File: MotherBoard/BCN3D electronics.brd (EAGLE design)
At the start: 70.5 x 95.8 mm, 87 parts, among them IC2 FT232RL, Q2 IRLS3034

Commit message: New File Tree and Updates
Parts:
- added DRILEGEND: (no value), drilegend:DRILEGEND
- U$5: device MarcEagleParts:SIGMA_LOGO -> MarcEagleParts:BCN3D_LOGO
- moved FID3 47.9 mm to (23.6, 9.93)
- moved LOGO1 21.3 mm to (16.1, 33.2)
- moved FID2 9.09 mm to (46.6, 79.9)
- moved U$5 3.98 mm to (25.6, 9.45)
- moved FID1 3.57 mm to (11.4, 67.2)
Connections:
- removed net 11111: ATMEGA2560.23
- removed net N$156: ATMEGA2560.38
- removed net N$157: ATMEGA2560.39
- removed net N$158: ATMEGA2560.40
- net GND: no longer U$1.GND
- net HOTEND2: now also ATMEGA2560.40
- net HOTEND3: now also ATMEGA2560.23
- net LFAN2: now also ATMEGA2560.39
- net LFAN3: now also ATMEGA2560.38
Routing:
- net +5V: track 226.6 -> 312.0 mm, vias 23 -> 22
- net LFAN2: track 0.00 -> 38.7 mm, vias 0 -> 2
- net HOTEND2: track 0.00 -> 38.7 mm, vias 0 -> 2
- net HOTEND3: track 0.00 -> 36.0 mm, vias 0 -> 4
- net LFAN3: track 0.00 -> 35.3 mm, vias 0 -> 2
- net GND: track 11.1 -> 24.5 mm, vias 43 -> 41
- net B-PWM: track 67.6 -> 69.0 mm, vias 2 -> 4
- net X-STEP: track 59.3 -> 58.2 mm, vias 1 -> 3
- net N$6: track 7.23 -> 8.26 mm
- net LCDRESET: track 74.2 -> 74.9 mm
- net LCDRX: track 73.0 -> 73.7 mm
- net LCDTX: track 71.6 -> 72.1 mm
- net R-PWM: track 66.3 -> 66.9 mm, vias 2 -> 4
- net X0-!EN: track 52.9 -> 53.4 mm
- net E3-!EN: track 48.3 -> 48.8 mm
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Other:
- board text added: "+"
- board text added: "+5V"
- board text added: "01-16"
- board text added: "01-20"
- board text added: "1"
- board text added: "2"
- board text added: "3"
- board text added: "4"
- board text added: "5"
- board text added: "6"
- board text added: "ATmega2560 TQFP 100"
- board text added: "AXIS ---------- 1 / 24V 2 / GND 3 / 5V 4 / !EN 5 / DIR 6 / STEP"
- board text added: "B"
- board text added: "BCN3D Electronics Designed in Barcelona ---------------------------------- MotherBoard - Nov 2014 Marc Cobler - REV_A"
- board text added: "CARRIAGE -------------- 1 / THERM 2 / HOTEND 3 / LFAN 4 / 5V 5 / GND 6 / 24V"
- board text added: "G"
- board text added: "GND"
- board text added: "LAYER-STACK"
- board text added: "NC"
- board text added: "Power Inductor"
- board text added: "R"
- board text added: "RST"
- board text added: "RX"
- board text added: "SIG"
- board text added: "TX"
- board text added: "V+"
- board text added: "gnd"
- board text added: "miso"
- board text added: "mosi"
- board text added: "sclk"
- board text added: "ss"
- board text removed: "ATmega2560"
- board text removed: "BCNelectronics - RepRapBCN Designed in Barcelona ---------------------------------- Sigma MotherBoard Marc Cobler - REV_A Nov 2014"
- board text removed: "RepRapBCN BCN3DSigma"

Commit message: Updates!
Rev_A Ready and firsts prototypes
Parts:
- F1: value PTCSMD -> IN_PTC
- renumbered PTC1 to F3
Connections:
- net GND: now also U$1.GND

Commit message: Updated files
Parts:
- removed USB: MINI-USB-SCHIELD, con-cypressindustries:32005-201
- added U$6: USB+SHIELD, SparkFun-Connectors:USB-B-PTH
- C7: value 4.7u -> 150UF; device rcl:C1206K -> MarcEagleParts:CAPAE660X610N
- D1: value MBRS140 -> (none); device MarcEagleParts:DO-214AA -> diode:SMC
- HOTBED: value (none) -> M025MM
- LED2, RXLED, TXLED: device adafruit:CHIP-LED0603 -> led:CHIPLED_0805
- moved C7 22.7 mm to (81.5, 16.2), turned to 0 degrees
- moved D1 21.0 mm to (81.4, 28.5), turned to 180 degrees
- moved C8 1.30 mm to (49.4, 14.3)
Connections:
- removed net N$84: F3.1, USB.1
- removed net USBSHIELD: L4.1, USB.5, USB.M1, USB.M2, USB.M3, USB.M4
- new net N$23: F3.1, U$6.VBUS
- net +24V: now also C8.+, LM2595.2; no longer C7.1, LM2595.1
- net +5V: now also C7.1; no longer C8.+
- net N$22: now also L4.1, U$6.GND, U$6.S1, U$6.S2; no longer USB.4
- net N$4: now also LM2595.1; no longer LM2595.2
- net USBD+: now also U$6.D+; no longer USB.3
- net USBD-: now also U$6.D-; no longer USB.2
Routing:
- net +24V: track 78.3 -> 33.3 mm, vias 14 -> 12
- net GND: track 24.5 -> 15.9 mm, vias 41 -> 40
- net N$84: track 8.33 -> 0.00 mm
- net +5V: track 312.0 -> 304.2 mm, vias 22 -> 21
- net N$4: track 42.6 -> 36.0 mm
- net USBSHIELD: track 6.15 -> 0.00 mm

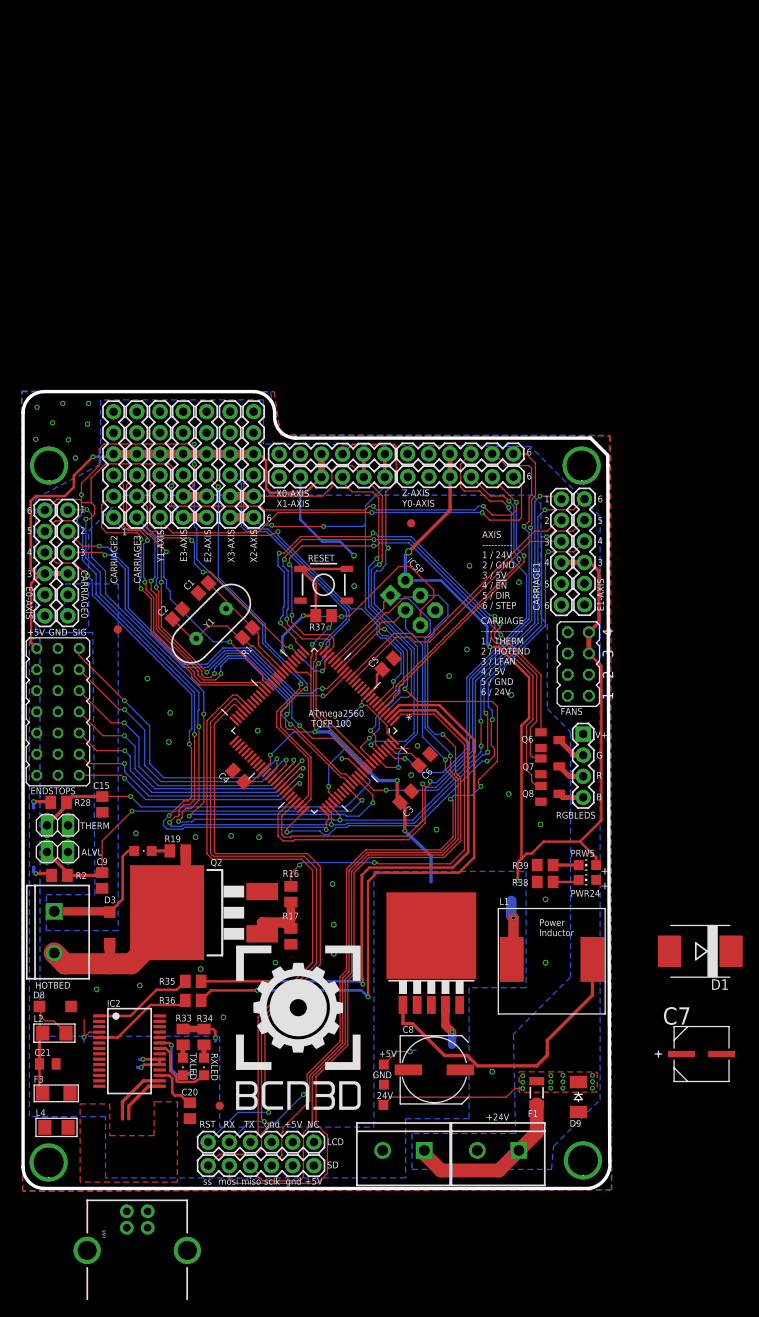
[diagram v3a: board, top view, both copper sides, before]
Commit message: The new REV_B has been shipped to production
New MainBoard Design, new Stepper drivers and new Extruder Board.
We also added many new components and configurations
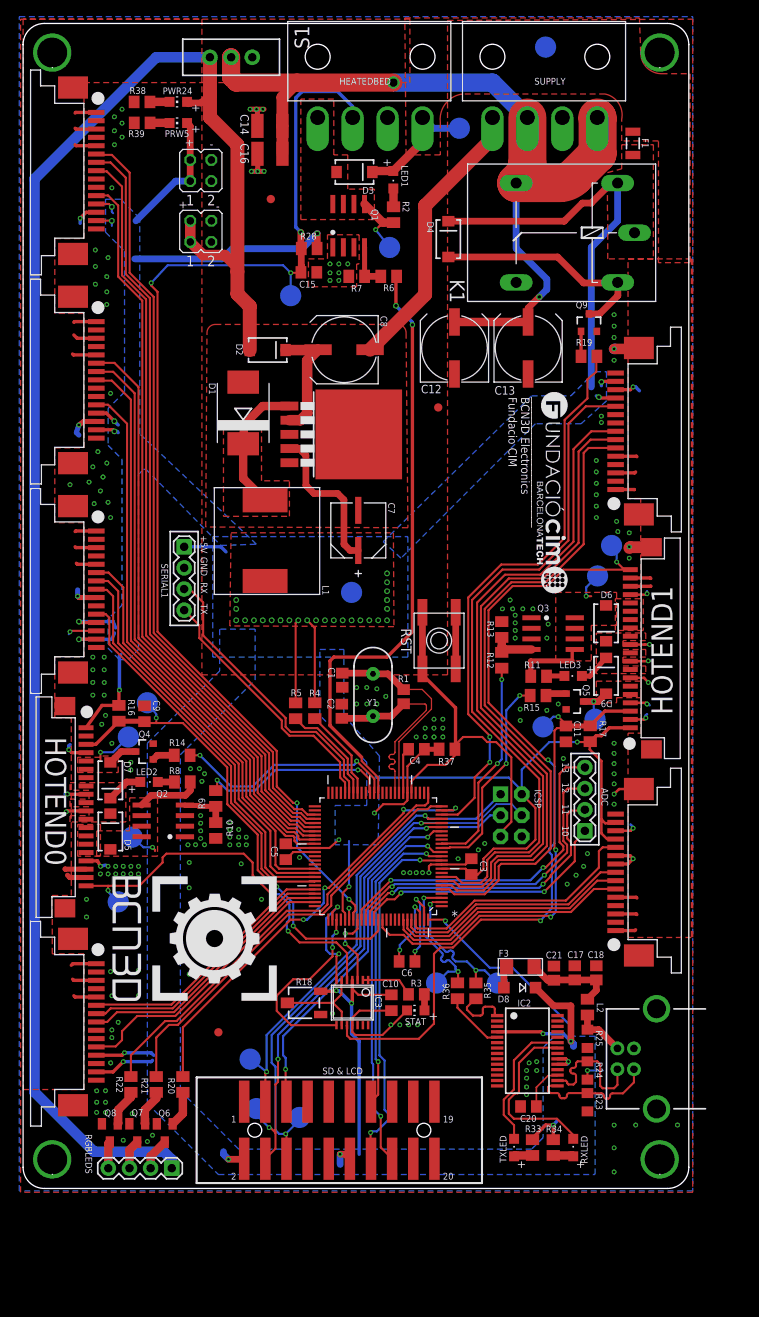
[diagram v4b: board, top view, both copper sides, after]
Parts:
- removed +24V: control, SparkFun-Connectors:SCREWTERMINAL-5MM-2
- removed +24V1: HEATED BED, SparkFun-Connectors:SCREWTERMINAL-5MM-2
- removed +5V, 24V, GND: (no value), testpad:TP12SQ
- removed ALVL, THERM: (no value), pinhead:1X02
- removed CARRIAGE0, CARRIAGE1, CARRIAGE2, CARRIAGE3, E0-AXIS, E1-AXIS, E2-AXIS, E3-AXIS, LCD, SD, X0-AXIS, X1-AXIS, X2-AXIS, X3-AXIS, Y0-AXIS, Y1-AXIS, Z-AXIS: (no value), MarcEagleParts:1X06
- removed DRILEGEND: (no value), drilegend:DRILEGEND
- removed ENDSTOPS: (no value), MarcEagleParts:MALE-PIN-3X7
- removed FANS: (no value), jumper:JP4Q
- removed HOTBED: M025MM, SparkFun-Connectors:SCREWTERMINAL-5MM-2
- removed L4: (no value), SAV MK-I:WUERTH-ELEKTRONIK_1206W
- removed RESET: SWITCHSMD, SparkFun-Electromechanical:TACTILE-SWITCH-SMD
- added ADC, SERIAL1: (no value), SparkFun-Connectors:1X04
- added C10: 100n, rcl:C0805
- added C11: 0.1u, rcl:C0805
- added C12, C13: 100u, rcl:UD-8X10_NICHICON
- added C14, C16: 10u, rcl:C1210K
- added C17: 4.7u, adafruit:C0805
- added C18: 10n, adafruit:C0805
- added D2, D4, D5, D6, D7: MBRA140, SparkFun-DiscreteSemi:SMA-DIODE
- added E0, E1, X0, X1, Y0, Z: FFC_15V_90G_1MM, MarcEagleParts:TE_FFC_CON1MM
- added HEATEDBED, SUPPLY: PC4WAY, MarcEagleParts:MOLEX_MINIFIT-JR
- added HOTEND0, HOTEND1: FFC_20V_90G_1MM", MarcEagleParts:SAMTEC_ZF1-T-WT
- added HTST1: HTST_20V_SMD_POL, MarcEagleParts:HTST-110-01-XX-DV
- added IC3: LMV324MZ, linear:TSSOP14
- added JP1: +5V, jumper:JP2Q
- added JP2: +24V, jumper:JP2Q
- added K1: G5L, relay:G5LE
- added LED1, LED3: (no value), led:CHIPLED_0805
- added Q1, Q3: MOSFET-N, MarcEagleParts:SOIC8
- added Q4, Q5, Q9: BC817, SparkFun-DiscreteSemi:SOT23-3
- added R10, R13, R4, R5, R7: 10K, rcl:M0805
- added R11, R8: 5.6k, rcl:M0805
- added R12, R14, R15, R20, R21, R22, R6, R9: 1K, rcl:M0805
- added R18: 10K, pot:3223J
- added R23, R24, R25: VARISTORCN0805, varistor:CT/CN0805
- added R3: 1K, rcl:R0805
- added RST: SPST_TACT-EVQQ2, adafruit:EVQ-Q2
- added S1: (no value), SparkFun-Electromechanical:SWITCH-SPDT
- added STAT: Orange, adafruit:CHIP-LED0805
- added TP1, TP10, TP11, TP12, TP13, TP14, TP15, TP16, TP17, TP18, TP2, TP3, TP4, TP5, TP6, TP7, TP8, TP9: TPB2,54, testpad:B2,54
- added U$7: (no value), MarcEagleParts:CC_LOGO
- added U$8: (no value), MarcEagleParts:BCN3D_LOGO
- added U$9: (no value), MarcEagleParts:FCIM_LOGO
- C21: value 10n -> 100n; device adafruit:C0805K -> adafruit:C0805
- D3: value MBR0520LT -> MBRA140; device diode:SOD123 -> SparkFun-DiscreteSemi:SMA-DIODE
- D9: value CGRM4004-G -> MBRA140; device diode:SOD-123_MINI-SMA -> SparkFun-DiscreteSemi:SMA-DIODE
- L2: value (none) -> 1800367 Ferrite Bead; device SAV MK-I:WUERTH-ELEKTRONIK_1206W -> rcl:M0805
- LED2: value HOTBED -> (none)
- Q2: value IRLS3034 -> MOSFET-N; device transistor-power:D2PACK -> MarcEagleParts:SOIC8
- R16: value 1K -> 4.7K
- R17: value 10K -> 4.7K
- R2: value 4.7K -> 5.6k
- R38: value 4.7K -> 5.6K
- moved U$3 152.3 mm to (76.5, 136.5)
- moved U$2 147.6 mm to (3.50, 136.5)
- moved F1 114.7 mm to (73.3, 125.6)
- moved U$4 111.1 mm to (76.5, 3.50)
- moved FID3 109.1 mm to (29.8, 118.9)
- moved PWR24 105.6 mm to (18.7, 130.6)
- moved R38 105.5 mm to (14.3, 130.6)
- moved U$1 104.9 mm to (3.50, 3.50)
- moved PRW5 101.8 mm to (18.7, 128.0)
- moved R39 101.5 mm to (14.3, 128.1)
- moved D3 95.5 mm to (39.8, 122.1), turned to 0 degrees
- moved R2 89.0 mm to (44.5, 117.0), turned to 90 degrees
- moved C8 87.2 mm to (38.6, 100.8), turned to 180 degrees
- moved D1 84.9 mm to (26.5, 93.2), turned to 90 degrees
- moved R19 77.3 mm to (68.0, 100.0), turned to 0 degrees
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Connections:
- net N$1 renamed XTAL_N
- net N$3 renamed XTAL_P
- net N$4 renamed OUT
- removed net AUTO_LEVEL: ALVL.1, ATMEGA2560.84, C9.1, R2.1
- removed net E-DIR: ATMEGA2560.77, E0-AXIS.5, E1-AXIS.5, E2-AXIS.5, E3-AXIS.5
- removed net E-STEP: ATMEGA2560.78, E0-AXIS.6, E1-AXIS.6, E2-AXIS.6, E3-AXIS.6
- removed net E2-!EN: ATMEGA2560.74, E2-AXIS.4
- removed net E3-!EN: ATMEGA2560.73, E3-AXIS.4
- removed net HOTEND2: ATMEGA2560.40, CARRIAGE2.2
- removed net HOTEND3: ATMEGA2560.23, CARRIAGE3.2
- removed net LFAN2: ATMEGA2560.39, CARRIAGE2.3
- removed net LFAN3: ATMEGA2560.38, CARRIAGE3.3
- removed net N$129: ATMEGA2560.12
- removed net N$130: ATMEGA2560.13
- removed net N$131 (its old number): ATMEGA2560.14
- removed net N$151: ATMEGA2560.83
- removed net N$152: ATMEGA2560.82
- removed net N$5: C21.1, F3.2, L2.2
- removed net N$83 (its old number): D8.A, L2.1
- removed net N$92: ATMEGA2560.54
- removed net N$93: ATMEGA2560.55
- removed net N$94: ATMEGA2560.56
- removed net N$95: ATMEGA2560.57
- removed net N$96: ATMEGA2560.58
- removed net N$97: ATMEGA2560.59
- removed net N$98: ATMEGA2560.60
- removed net THERM0: ATMEGA2560.87, CARRIAGE0.1
- removed net THERM1: ATMEGA2560.88, CARRIAGE1.1
- removed net THERM2: ATMEGA2560.86, CARRIAGE2.1
- removed net THERM3: ATMEGA2560.85, CARRIAGE3.1
- removed net USBD+: IC2.15, U$6.D+
- removed net USBD-: IC2.16, U$6.D-
- removed net X-DIR: ATMEGA2560.95, X0-AXIS.5, X1-AXIS.5, X2-AXIS.5, X3-AXIS.5
- removed net X-STEP: ATMEGA2560.96, X0-AXIS.6, X1-AXIS.6, X2-AXIS.6, X3-AXIS.6
- removed net X2-!EN: ATMEGA2560.92, X2-AXIS.4
- removed net X2-STOP: ATMEGA2560.67, ENDSTOPS.5
- removed net X3-!EN: ATMEGA2560.91, X3-AXIS.4
- removed net X3-STOP: ATMEGA2560.68, ENDSTOPS.6
- removed net Y0-!EN: ATMEGA2560.6, Y0-AXIS.4
- removed net Y0-STOP: ATMEGA2560.65, ENDSTOPS.3
- removed net Y1-!EN: ATMEGA2560.7, Y1-AXIS.4
- removed net Y1-STOP: ATMEGA2560.66, ENDSTOPS.4
- new net 24VBF: F1.1, K1.P
- new net ADC10: ADC.1, ATMEGA2560.87
- new net ADC11: ADC.2, ATMEGA2560.86
- new net ADC12: ADC.3, ATMEGA2560.85
- new net ADC13: ADC.4, ATMEGA2560.84
- new net ATLVL0: HOTEND0.20, IC3.5, TP4.TP
- new net ATLVL1: HOTEND1.20, IC3.10, TP5.TP
- new net E0-DIR: ATMEGA2560.71, E0.6
- new net E0-STEP: ATMEGA2560.73, E0.8
- new net E0-STOP: ATMEGA2560.74, E0.11
- new net E1-DIR: ATMEGA2560.94, E1.6
- new net E1-STEP: ATMEGA2560.96, E1.8
- new net E1-STOP: ATMEGA2560.97, E1.11
- new net H0-STOP: ATMEGA2560.77, IC3.7
- new net H1-STOP: ATMEGA2560.78, IC3.8
- new net HOTBED: D3.A, HEATEDBED.4, Q1.5, Q1.6, Q1.7, Q1.8, R2.1, TP6.TP
- new net HOTEND0_THERM: ATMEGA2560.88, C9.1, HOTEND0.3, R16.1, TP12.TP
- new net HOTEND1_THERM: ATMEGA2560.89, C11.1, HOTEND1.3, R17.1, TP11.TP
- new net LMIN: C8.+, D2.C, LM2595.2
- new net MLED: ATMEGA2560.83, IC3.3
- new net N$100: D4.A, K1.2, Q9.3
- new net N$102: LED3.C, R11.2
- new net N$103: Q3.4, R12.1, R13.1
- new net N$107: Q5.1, R15.1
- new net N$108: C12.+, C13.+, C14.1, C16.1, K1.S, S1.2, SUPPLY.1, SUPPLY.3
- new net N$110: IC3.6, IC3.9, R18.2
- new net N$111: HTST1.8
- new net N$112: HTST1.9
- new net N$114: ATMEGA2560.63
- new net N$115: HTST1.10
- new net N$116: HTST1.16
- new net N$117: HTST1.17
- new net N$118: HTST1.18
- new net N$119: HTST1.19
- new net N$120: HTST1.20
- new net N$121: S1.1
- new net N$122: ATMEGA2560.64
- new net N$123: ATMEGA2560.17
- new net N$124: ATMEGA2560.18
- new net N$126: ATMEGA2560.65
- new net N$26: IC3.1, IC3.2, R3.2
- new net N$27: Q6.1, R20.1
- new net N$28: R3.1, STAT.A
- new net N$29: ATMEGA2560.76
- new net N$31: Q7.1, R21.1
- new net N$32: Q8.1, R22.1
- new net N$33: ATMEGA2560.75
- new net N$73: ATMEGA2560.92
- new net N$74: ATMEGA2560.91
- new net N$75: ATMEGA2560.90
- new net N$90: Q4.1, R14.1
- new net N$99: Q2.4, R10.1, R9.1
- new net PWM_HOTEND0: ATMEGA2560.40, R9.2
- new net PWM_HOTEND1: ATMEGA2560.16, R12.2
- new net PWM_LFAN0: ATMEGA2560.39, R14.2
- new net PWM_LFAN1: ATMEGA2560.15, R15.2
- new net RELAY: ATMEGA2560.23, R19.2
- new net RX1: ATMEGA2560.45, SERIAL1.3
- new net TX1: ATMEGA2560.46, SERIAL1.4
- new net USBD+_P: IC2.15, R23.1, U$6.D+
- new net USBD-_N: IC2.16, R24.1, U$6.D-
- new net VBUS: L2.2, R25.1, U$6.VBUS
- new net VBUSAF: C17.1, C18.1, C21.1, F3.2, L2.1
- new net VCC2: D2.A, JP2.1, JP2.3, PWR24.A, RGBLEDS.1, S1.3
- new net X0-DIR: ATMEGA2560.66, X0.6
- new net X0-STEP: ATMEGA2560.68, X0.8
- new net X1-DIR: ATMEGA2560.5, X1.6
- new net X1-STEP: ATMEGA2560.7, X1.8
- new net Y-!EN: ATMEGA2560.58, Y0.7
- new net Y-STOP: ATMEGA2560.60, Y0.11
- net !RESET: now also RST.A, RST.A'; no longer RESET.1, RESET.2
- net +24V: now also D5.C, D6.C, D7.C, E0.1, E0.3, E0.5, E1.1, E1.3, E1.5, HEATEDBED.1, HOTEND0.10, HOTEND0.12, HOTEND0.18, HOTEND0.19, HOTEND0.8, HOTEND1.10, HOTEND1.12, HOTEND1.18, HOTEND1.19, HOTEND1.8, HOTEND1.GND1, LED1.A, LED3.A, TP2.TP, X0.1, X0.3, X0.5, X1.1, X1.3, X1.5, Y0.1, Y0.3, Y0.5, Z.1, Z.3, Z.5, Z.GND@1; no longer 24V.TP, C8.+, CARRIAGE0.6, CARRIAGE1.6, CARRIAGE2.6, CARRIAGE3.6, E0-AXIS.1, E1-AXIS.1, E2-AXIS.1, E3-AXIS.1, FANS.1, FANS.3, HOTBED.1, LM2595.2, PWR24.A, RGBLEDS.1, X0-AXIS.1, X1-AXIS.1, X2-AXIS.1, X3-AXIS.1, Y0-AXIS.1, Y1-AXIS.1, Z-AXIS.1
- net +5V: now also C10.1, D4.C, E0.12, E0.14, E1.12, E1.14, HOTEND0.1, HOTEND1.1, HTST1.1, HTST1.11, IC3.4, JP1.1, JP1.3, K1.1, R16.2, R17.2, R18.3, R4.1, R5.1, SERIAL1.1, TP3.TP, X0.12, X0.14, X1.12, X1.14, Y0.12, Y0.14, Z.12, Z.14; no longer +5V.TP, CARRIAGE0.4, CARRIAGE1.4, CARRIAGE2.4, CARRIAGE3.4, E0-AXIS.3, E1-AXIS.3, E2-AXIS.3, E3-AXIS.3, ENDSTOPS.15, ENDSTOPS.16, ENDSTOPS.17, ENDSTOPS.18, ENDSTOPS.19, ENDSTOPS.20, ENDSTOPS.21, FANS.5, FANS.7, LCD.5, R2.2, SD.6, X0-AXIS.3, X1-AXIS.3, X2-AXIS.3, X3-AXIS.3, Y0-AXIS.3, Y1-AXIS.3, Z-AXIS.3
- net B-PWM: now also R22.2; no longer Q8.1
- net BED_THERM: now also ATMEGA2560.82, HEATEDBED.3, TP18.TP; no longer ATMEGA2560.89, THERM.1
- net E0-!EN: now also ATMEGA2560.72, E0.7; no longer ATMEGA2560.76, E0-AXIS.4
- net E1-!EN: now also ATMEGA2560.95, E1.7; no longer ATMEGA2560.75, E1-AXIS.4
- net G-PWM: now also R20.2; no longer Q6.1
- net GND: now also C10.2, C11.2, C12.-, C13.-, C14.2, C16.2, C17.2, C18.2, E0.10, E0.13, E0.15, E0.2, E0.4, E0.9, E0.GND@1, E0.GND@2, E1.10, E1.13, E1.15, E1.2, E1.4, E1.9, E1.GND@1, E1.GND@2, HEATEDBED.2, HOTEND0.11, HOTEND0.17, HOTEND0.2, HOTEND0.4, HOTEND0.7, HOTEND0.9, HOTEND0.GND1, HOTEND0.GND2, HOTEND1.11, HOTEND1.17, HOTEND1.2, HOTEND1.4, HOTEND1.7, HOTEND1.9, HOTEND1.GND2, HTST1.12, HTST1.2, IC3.11, JP1.2, JP1.4, JP2.2, JP2.4, Q1.1, Q1.2, Q1.3, Q2.1, Q2.2, Q3.1, Q3.2, Q3.3, Q4.2, Q5.2, Q9.2, R10.2, R13.2, R18.1, R23.2, R24.2, R25.2, R7.2, RST.B, RST.B', SERIAL1.2, STAT.C, SUPPLY.2, SUPPLY.4, TP1.TP, U$6.GND, U$6.S1, U$6.S2, X0.10, X0.13, X0.15, X0.2, X0.4, X0.9, X0.GND@1, X0.GND@2, X1.10, X1.13, X1.15, X1.2, X1.4, X1.9, X1.GND@1, X1.GND@2, Y0.10, Y0.13, Y0.15, Y0.2, Y0.4, Y0.9, Y0.GND@1, Y0.GND@2, Z.10, Z.13, Z.15, Z.2, Z.4, Z.9, Z.GND@2; no longer +24V.2, +24V1.2, ALVL.2, CARRIAGE0.5, CARRIAGE1.5, CARRIAGE2.5, CARRIAGE3.5, D9.A, E0-AXIS.2, E1-AXIS.2, E2-AXIS.2, E3-AXIS.2, ENDSTOPS.10, ENDSTOPS.11, ENDSTOPS.12, ENDSTOPS.13, ENDSTOPS.14, ENDSTOPS.8, ENDSTOPS.9, FANS.2, FANS.4, FANS.6, FANS.8, GND.TP, L4.2, LCD.4, R17.2, RESET.3, RESET.4, SD.5, THERM.2, X0-AXIS.2, X1-AXIS.2, X2-AXIS.2, X3-AXIS.2, Y0-AXIS.2, Y1-AXIS.2, Z-AXIS.2
- net HOTEND0: now also D5.A, HOTEND0.13, HOTEND0.14, HOTEND0.15, HOTEND0.16, Q2.5, Q2.6, Q2.7, Q2.8, R8.1, TP7.TP; no longer ATMEGA2560.18, CARRIAGE0.2
- net HOTEND1: now also D6.A, HOTEND1.13, HOTEND1.14, HOTEND1.15, HOTEND1.16, Q3.5, Q3.6, Q3.7, Q3.8, R11.1, TP8.TP; no longer ATMEGA2560.16, CARRIAGE1.2
- net LCDRESET: now also ATMEGA2560.14, HTST1.15; no longer ATMEGA2560.47, LCD.1
- net LCDRX: now also ATMEGA2560.13, HTST1.14; no longer ATMEGA2560.46, LCD.2
- net LCDTX: now also ATMEGA2560.12, HTST1.13; no longer ATMEGA2560.45, LCD.3
- net LFAN0: now also D7.A, HOTEND0.5, HOTEND0.6, Q4.3, TP9.TP; no longer ATMEGA2560.17, CARRIAGE0.3
- net LFAN1: now also D9.A, HOTEND1.5, HOTEND1.6, Q5.3, TP10.TP; no longer ATMEGA2560.15, CARRIAGE1.3
- net MISO: now also HTST1.4, TP16.TP; no longer SD.3
- net MOSI: now also HTST1.5, TP15.TP; no longer SD.2
- net N$113: now also ATMEGA2560.1; no longer ATMEGA2560.8
- net N$22: now also ATMEGA2560.47; no longer L4.1, U$6.GND, U$6.S1, U$6.S2
- net N$23: now also D8.A; no longer U$6.VBUS
- net N$24: now also HTST1.7; no longer LCD.6
- net N$25: now also Q9.1, R19.1; no longer +24V.1, +24V1.1, F1.1
- net N$63: now also LED1.C, R2.2; no longer Q2.1, R16.1, R17.1
- net N$66: now also Q1.4, R6.1, R7.1; no longer D3.A, HOTBED.2, Q2.2, R19.1
- net N$69: now also ATMEGA2560.93; no longer LED2.C, R19.2
- net N$91: now also LED2.C, R8.2; no longer ATMEGA2560.53
- net PWM_HOTBED: now also ATMEGA2560.38, R6.2; no longer ATMEGA2560.1, R16.2
- net R-PWM: now also R21.2; no longer Q7.1
- net RX0: now also TP13.TP
- net SCL: now also R4.2
- net SCLK: now also HTST1.3, TP17.TP; no longer SD.4
- net SDA: now also R5.2
- net SDSS: now also HTST1.6; no longer SD.1
- net TX0: now also TP14.TP
- net X0-!EN: now also ATMEGA2560.67, X0.7; no longer ATMEGA2560.94, X0-AXIS.4
- net X0-STOP: now also ATMEGA2560.69, X0.11; no longer ATMEGA2560.63, ENDSTOPS.1
- net X1-!EN: now also ATMEGA2560.6, X1.7; no longer ATMEGA2560.93, X1-AXIS.4
- net X1-STOP: now also ATMEGA2560.8, X1.11; no longer ATMEGA2560.64, ENDSTOPS.2
- net Y-DIR: now also ATMEGA2560.57, Y0.6; no longer ATMEGA2560.5, Y0-AXIS.5, Y1-AXIS.5
- net Y-STEP: now also ATMEGA2560.59, Y0.8; no longer ATMEGA2560.90, Y0-AXIS.6, Y1-AXIS.6
- net Z-!EN: now also ATMEGA2560.54, Z.7; no longer ATMEGA2560.97, Z-AXIS.4
- net Z-DIR: now also ATMEGA2560.53, Z.6; no longer ATMEGA2560.71, Z-AXIS.5
- net Z-STEP: now also ATMEGA2560.55, Z.8; no longer ATMEGA2560.72, Z-AXIS.6
- net Z-STOP: now also ATMEGA2560.56, Z.11; no longer ATMEGA2560.69, ENDSTOPS.7
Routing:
- net VCC2: track 0.00 -> 208.3 mm
- net E-DIR: track 158.7 -> 0.00 mm, vias 10 -> 0
- net E-STEP: track 155.5 -> 0.00 mm, vias 8 -> 0
- net GND: track 15.9 -> 151.9 mm, vias 40 -> 215
- net N$108: track 0.00 -> 101.0 mm, vias 0 -> 2
- net ATLVL1: track 0.00 -> 100.7 mm, vias 0 -> 3
- net BED_THERM: track 50.1 -> 139.6 mm, vias 2 -> 5
- net X1-STEP: track 0.00 -> 79.6 mm
- net X1-DIR: track 0.00 -> 78.9 mm
- net +5V: track 304.2 -> 381.9 mm, vias 21 -> 50
- net THERM0: track 72.4 -> 0.00 mm, vias 4 -> 0
- net Y-!EN: track 0.00 -> 69.2 mm
- net RELAY: track 0.00 -> 68.8 mm, vias 0 -> 2
- net Y-STOP: track 0.00 -> 66.2 mm
- net SDSS: track 107.2 -> 42.4 mm, vias 6 -> 2
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- added copper zone on layer 1, net +5V
- added copper zone on layer 1, net 24VBF
- added copper zone on layer 1, net HOTBED
- added copper zone on layer 1, net HOTEND0
- added copper zone on layer 1, net HOTEND1
- added copper zone on layer 1, net LFAN0
- added copper zone on layer 1, net LFAN1
- added copper zone on layer 1, net OUT
- removed copper zone on layer 16, net +24V
- removed copper zone on layer 1, net USBSHIELD
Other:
- board size 70.5 x 95.8 mm -> 80 x 140 mm
- board text added: "-"
- board text added: "10"
- board text added: "11"
- board text added: "12"
- board text added: "13"
- board text added: "19"
- board text added: "20"
- board text added: "BCN3D Electronics MainBoard v1.0 Designed in Barcelona ___________________ MotherBoard - Jan 2015 Marc Cobler - REV_B ___________________"
- board text added: "SD & LCD"
- board text added: "_________________________ BCN3D Electronics Fundacio CIM"
- board text removed: "3"
- board text removed: "4"
- board text removed: "5"
- board text removed: "6"
- board text removed: "ATmega2560 TQFP 100"
- board text removed: "AXIS ---------- 1 / 24V 2 / GND 3 / 5V 4 / !EN 5 / DIR 6 / STEP"
- board text removed: "B"
- board text removed: "BCN3D Electronics Designed in Barcelona ---------------------------------- MotherBoard - Nov 2014 Marc Cobler - REV_A"
- board text removed: "CARRIAGE -------------- 1 / THERM 2 / HOTEND 3 / LFAN 4 / 5V 5 / GND 6 / 24V"
- board text removed: "G"
- board text removed: "LAYER-STACK"
- board text removed: "NC"
- board text removed: "Power Inductor"
- board text removed: "R"
- board text removed: "RST"
- board text removed: "SIG"
- board text removed: "V+"
- board text removed: "gnd"
- board text removed: "miso"
- board text removed: "mosi"
- board text removed: "sclk"
- board text removed: "ss"

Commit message: BCN3D Electronics REV.E tested and manufactured
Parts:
- removed HTST1: HTST_20V_SMD_POL, MarcEagleParts:HTST-110-01-XX-DV
- removed JP1: +5V, jumper:JP2Q
- removed JP2: +24V, jumper:JP2Q
- removed PRW5: Red, adafruit:CHIP-LED0805
- removed RST: SPST_TACT-EVQQ2, adafruit:EVQ-Q2
- removed S1: (no value), SparkFun-Electromechanical:SWITCH-SPDT
- removed SERIAL1: (no value), SparkFun-Connectors:1X04
- removed TP14, TP18, TP6: TPB2,54, testpad:B2,54
- removed U$2, U$3, U$4: SANGUINOLOLU_PLATED-SCREW, SAV MK-I:SANGUINOLOLU_PLATEDSCREW
- added +24V, +5V: (no value), jumper:JP2Q
- added C19: 100n, rcl:C0805
- added C22, C23: 0.1u, rcl:C0805
- added C24: 100n, adafruit:C0805
- added C25: 10n, rcl:C0805
- added D10: MBR0520LT, diode:SOD123
- added I2C, LEDS1, UART1: (no value), SparkFun-Connectors:1X04
- added IC1: LM358D, linear:SO08
- added L10, L11, L12, L13, L14, L15, L16, L17, L18, L19, L20, L21, L3, L4, L5, L6, L7, L8, L9: (no value), EagleLibrary_Wuerth_Elektronik_eiSos_V6_20140807:0805
- added LCD, SD: (no value), pinhead:1X06
- added PWR5: Blue, led:CHIPLED_0805
- added R26, R29: 4.7K, rcl:M0805
- added R27, R30, R43, R45, R46, R47: 1K, rcl:M0805
- added R31, R40, R42: 10K, rcl:M0805
- added R32: 330, adafruit:M0805
- added R41: 20K, rcl:M0805
- added R44: 100K, rcl:M0805
- added RESET: SPST, adafruit:EVQ-Q2
- added RSHUNT: 10m, SparkFun-Resistors:R2512
- added SH1: SHORTT5, shorts:SHORT_TOP-50
- added SJ1: (no value), jumper:SJ
- added TP19, TP20, TP21, TP22, TP23, TP24, TP25, TP26, TP27, TP28, TP29, TP30, TP31, TP32, TP33, TP34, TP35, TP36, TP37, TP38: TPB2,54, testpad:B2,54
- added U1: INA169, SparkFun-AnalogIC:SOT23-5
- added VCC2: (no value), jumper:JP1
- C11, C15, C9: value 0.1u -> 10u
- HOTEND0, HOTEND1: value FFC_20V_90G_1MM" -> FFC_20V_90G_1MM3; device MarcEagleParts:SAMTEC_ZF1-T-WT -> MarcEagleParts:FCI_20WAY_1MM_3ST
- IC3: value LMV324MZ -> LM311D; device linear:TSSOP14 -> linear:SO08
- ICSP: value (none) -> AVR_SPI_PRG_6NS
- L2: value 1800367 Ferrite Bead -> (none); device rcl:M0805 -> EagleLibrary_Wuerth_Elektronik_eiSos_V6_20140807:0805
- LED1, LED2, LED3: value (none) -> Blue
- LM2595: device linear:TO263-5 -> MarcEagleParts:TO263-5
- PWR24: value Red -> Blue; device adafruit:CHIP-LED0805 -> led:CHIPLED_0805
- Q1, Q2, Q3: value MOSFET-N -> MOSFET-NSOIC8
- Q4, Q5, Q9: value BC817 -> MMBT2222A
- R1: value 1M -> 10K; device resistor:R0805 -> rcl:M0805
- R18: device pot:3223J -> rcl:M0805
- R4, R5: value 10K -> 4.7k
- U$1: value SANGUINOLOLU_PLATED-SCREW -> (none); device SAV MK-I:SANGUINOLOLU_PLATEDSCREW -> MarcEagleParts:BCN3D_QR
- moved Z 114.0 mm to (4.00, 18.3)
- moved U$1 112.6 mm to (60.4, 100.7), flipped to the bottom, turned to 270 degrees
- moved FID1 93.4 mm to (69.2, 2.48)
- moved IC3 89.9 mm to (33.7, 112.0), turned to 270 degrees
- moved TP13 83.4 mm to (24.1, 101.3), turned to 0 degrees
- moved TP5 73.1 mm to (48.1, 7.77), turned to 90 degrees
- moved Y0 71.3 mm to (76.0, 120.8), turned to 90 degrees
- moved F1 65.2 mm to (8.13, 129.0), turned to 180 degrees
- moved TP1 55.8 mm to (7.12, 133.7), turned to 0 degrees
- moved SUPPLY 47.2 mm to (21.9, 132.4)
- moved R1 47.1 mm to (44.8, 106.2), turned to 180 degrees
- moved K1 46.3 mm to (17.7, 115.3), turned to 0 degrees
- moved C13 44.6 mm to (16.7, 93.5), turned to 0 degrees
- moved TP2 42.5 mm to (10.4, 133.7), turned to 0 degrees
- moved D4 42.3 mm to (10.1, 103.9)
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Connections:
- removed net ATLVL0: HOTEND0.20, IC3.5, TP4.TP
- removed net ATLVL1: HOTEND1.20, IC3.10, TP5.TP
- removed net H0-STOP: ATMEGA2560.77, IC3.7
- removed net H1-STOP: ATMEGA2560.78, IC3.8
- removed net N$108: C12.+, C13.+, C14.1, C16.1, K1.S, S1.2, SUPPLY.1, SUPPLY.3
- removed net N$110: IC3.6, IC3.9, R18.2
- removed net N$111: HTST1.8
- removed net N$112: HTST1.9
- removed net N$115: HTST1.10
- removed net N$116: HTST1.16
- removed net N$117: HTST1.17
- removed net N$118: HTST1.18
- removed net N$119: HTST1.19
- removed net N$120: HTST1.20
- removed net N$121: S1.1
- removed net N$124: ATMEGA2560.18
- removed net N$146: ATMEGA2560.41
- removed net N$25: Q9.1, R19.1
- removed net RX0: ATMEGA2560.2, R35.1, TP13.TP
- removed net TX0: ATMEGA2560.3, R36.1, TP14.TP
- removed net VBUSAF: C17.1, C18.1, C21.1, F3.2, L2.1
- new net 24VINA: K1.P, RSHUNT.1, U1.3
- new net BED_THERM_CON: HEATEDBED.3, R45.1
- new net EARTH: L21.2, U$6.S1, U$6.S2
- new net GUARD: C1.2, C2.2, SH1.2
- new net HOTEND0_THERM_CON: HOTEND0.3, R46.1
- new net HOTEND1_THERM_CON: HOTEND1.3, R47.1
- new net INA_OUT: IC3.3, R41.2, U1.1
- new net N$1: C19.1, IC2.2
- new net N$34: L13.1, X0.7
- new net N$35: L14.1, X0.9
- new net N$36: L18.1, Y0.6
- new net N$37: L19.1, Y0.7
- new net N$39: L20.1, Y0.9
- new net N$4: ATMEGA2560.14
- new net N$40: L15.1, X1.6
- new net N$41: L16.1, X1.7
- new net N$42: L17.1, X1.9
- new net N$43: E0.6, L6.2
- new net N$44: E0.7, L7.2
- new net N$45: E0.9, L8.2
- new net N$47: ATMEGA2560.55
- new net N$48: F3.2, L2.1
- new net N$49: IC3.2, R1.2, R42.1, R44.1
- new net N$5: L12.1, X0.6
- new net N$54: L3.1, Z.6
- new net N$55: L4.1, Z.7
- new net N$56: L5.1, Z.9
- new net N$57: E1.9, L11.1
- new net N$58: E1.7, L10.1
- new net N$59: E1.6, L9.1
- new net RELAYINA: IC3.7, Q9.1, R19.1, R43.2, R44.2, SJ1.1, SJ1.2
- new net SUPPLY: C12.+, C13.+, C14.1, C16.1, K1.S, LEDS1.1, PWR24.A, RGBLEDS.1, SUPPLY.1, SUPPLY.3, TP2.TP, VCC2.1
- new net UART_N: ATMEGA2560.3, R36.1
- new net UART_P: ATMEGA2560.2, R35.1
- new net Z0-ENDSTOP: HOTEND0.20, R26.1, R27.1
- new net Z0-STOP: ATMEGA2560.56, C22.1, R27.2
- new net Z1-ENDSTOP: HOTEND1.20, R29.1, R30.1
- new net Z1-STOP: ATMEGA2560.41, C23.1, R30.2
- net !RESET: now also C19.2, C25.1, D10.A, R32.1; no longer RST.A, RST.A'
- net +24V: now also Y0.GND@2; no longer HOTEND1.GND1, TP2.TP, Z.GND@1
- net +5V: now also +24V.1, +24V.3, C17.1, C18.1, C21.1, C24.1, D10.C, I2C.1, IC1.8, IC3.8, LCD.1, PWR5.A, R1.1, R26.2, R29.2, R43.1, SD.6, U1.5, UART1.1; no longer HTST1.1, HTST1.11, IC3.4, JP1.1, JP1.3, PRW5.A, R18.3, SERIAL1.1
- net 24VBF: now also RSHUNT.2, U1.4; no longer K1.P
- net BED_THERM: now also R45.2, TP13.TP; no longer HEATEDBED.3, TP18.TP
- net E0-!EN: now also L7.1, TP34.TP; no longer E0.7
- net E0-DIR: now also ATMEGA2560.73, L8.1, TP33.TP; no longer ATMEGA2560.71, E0.6
- net E0-STEP: now also ATMEGA2560.71, L6.1, TP35.TP; no longer ATMEGA2560.73, E0.8
- net E1-!EN: now also L10.2, TP31.TP; no longer E1.7
- net E1-DIR: now also ATMEGA2560.96, L11.2, TP32.TP; no longer ATMEGA2560.94, E1.6
- net E1-STEP: now also ATMEGA2560.94, L9.2, TP30.TP; no longer ATMEGA2560.96, E1.8
- net GND: now also +24V.2, +24V.4, +5V.2, +5V.4, C22.2, C23.2, C24.2, C25.2, E0.8, E1.8, HOTEND1.GND1, I2C.2, IC1.4, IC3.1, IC3.4, L21.1, LCD.4, LCD.6, R18.2, R31.2, R40.2, R41.1, R42.2, RESET.A, RESET.A', SD.1, SH1.1, U1.2, UART1.2, X0.8, X1.8, Y0.8, Z.8, Z.GND@1; no longer C1.2, C2.2, E0.9, E1.9, HTST1.12, HTST1.2, IC3.11, JP1.2, JP1.4, JP2.2, JP2.4, R18.1, RST.B, RST.B', SERIAL1.2, U$1.GND, U$2.GND, U$3.GND, U$4.GND, U$6.S1, U$6.S2, X0.9, X1.9, Y0.9, Y0.GND@2, Z.9
- net HOTBED: no longer TP6.TP
- net HOTEND0_THERM: now also R46.2; no longer HOTEND0.3
- net HOTEND1_THERM: now also R47.2; no longer HOTEND1.3
- net LCDRESET: now also ATMEGA2560.18, LCD.5, TP4.TP; no longer ATMEGA2560.14, HTST1.15
- net LCDRX: now also LCD.3, TP5.TP; no longer HTST1.14
- net LCDTX: now also LCD.2, TP15.TP; no longer HTST1.13
- net MISO: now also SD.2, TP20.TP; no longer HTST1.4, TP16.TP
- net MLED: now also IC1.3; no longer IC3.3
- net MOSI: now also SD.4, TP17.TP; no longer HTST1.5, TP15.TP
- net N$10: now also LEDS1.3
- net N$11: now also LEDS1.4
- net N$13: now also R32.2, RESET.B, RESET.B'; no longer IC2.2
- net N$162: now also PWR5.C; no longer PRW5.C
- net N$23: now also L2.2; no longer F3.1
- net N$24: now also ATMEGA2560.78; no longer HTST1.7
- net N$26: now also IC1.1, IC1.2; no longer IC3.1, IC3.2
- net N$27: now also R18.1
- net N$29: now also ATMEGA2560.53; no longer ATMEGA2560.76
- net N$31: now also R31.1
- net N$32: now also R40.1
- net N$33: now also ATMEGA2560.54; no longer ATMEGA2560.75
- net N$9: now also LEDS1.2
- net RX1: now also UART1.3; no longer SERIAL1.3
- net SCL: now also I2C.3
- net SCLK: now also SD.3, TP19.TP; no longer HTST1.3, TP17.TP
- net SDA: now also I2C.4
- net SDSS: now also SD.5, TP16.TP; no longer HTST1.6
- net TX1: now also UART1.4; no longer SERIAL1.4
- net VBUS: now also F3.1; no longer L2.2
- net VCC2: now also +5V.1, +5V.3, VCC2.2; no longer JP2.1, JP2.3, PWR24.A, RGBLEDS.1, S1.3
- net X0-!EN: now also L13.2, TP22.TP; no longer X0.7
- net X0-DIR: now also ATMEGA2560.68, L14.2, TP23.TP; no longer ATMEGA2560.66, X0.6
- net X0-STEP: now also ATMEGA2560.66, L12.2, TP21.TP; no longer ATMEGA2560.68, X0.8
- net X1-!EN: now also L16.2, TP25.TP; no longer X1.7
- net X1-DIR: now also ATMEGA2560.7, L17.2, TP26.TP; no longer ATMEGA2560.5, X1.6
- net X1-STEP: now also ATMEGA2560.5, L15.2, TP24.TP; no longer ATMEGA2560.7, X1.8
- net XTAL_N: no longer R1.2
- net XTAL_P: no longer R1.1
- net Y-!EN: now also ATMEGA2560.59, L19.2, TP28.TP; no longer ATMEGA2560.58, Y0.7
- net Y-DIR: now also ATMEGA2560.58, L20.2, TP29.TP; no longer ATMEGA2560.57, Y0.6
- net Y-STEP: now also ATMEGA2560.60, L18.2, TP27.TP; no longer ATMEGA2560.59, Y0.8
- net Y-STOP: now also ATMEGA2560.57; no longer ATMEGA2560.60
- net Z-!EN: now also ATMEGA2560.76, L4.2, TP37.TP; no longer ATMEGA2560.54, Z.7
- net Z-DIR: now also ATMEGA2560.77, L5.2, TP36.TP; no longer ATMEGA2560.53, Z.6
- net Z-STEP: now also ATMEGA2560.75, L3.2, TP38.TP; no longer ATMEGA2560.55, Z.8
- net Z-STOP: no longer ATMEGA2560.56
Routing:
- net SUPPLY: track 0.00 -> 198.5 mm, vias 0 -> 6
- net VCC2: track 208.3 -> 24.1 mm
- net N$108: track 101.0 -> 0.00 mm, vias 2 -> 0
- net ATLVL1: track 100.7 -> 0.00 mm, vias 3 -> 0
- net Z-STOP: track 88.9 -> 0.00 mm
- net GND: track 151.9 -> 64.2 mm, vias 215 -> 234
- net Z-STEP: track 91.1 -> 18.8 mm, vias 0 -> 1
- net Z-!EN: track 91.9 -> 22.0 mm, vias 0 -> 1
- net Z-DIR: track 92.4 -> 22.8 mm, vias 0 -> 1
- net Z1-STOP: track 0.00 -> 54.1 mm, vias 0 -> 2
- net ATLVL0: track 47.0 -> 0.00 mm, vias 3 -> 0
- net GUARD: track 0.00 -> 45.0 mm, vias 0 -> 8
- net BED_THERM: track 139.6 -> 95.7 mm, vias 5 -> 3
- net Y-STOP: track 66.2 -> 105.9 mm, vias 0 -> 2
- net 24VINA: track 0.00 -> 39.3 mm, vias 0 -> 2
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- added copper zone on layer 1, net 24VINA
- added copper zone on layer 1, net EARTH
- added copper zone on layer 16, net EARTH
- added copper zone on layer 16, net GUARD
- added copper zone on layer 1, net SUPPLY
- added copper zone on layer 16, net SUPPLY
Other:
- board text added: "*"
- board text added: "+24V"
- board text added: "24V"
- board text added: "2A MAX"
- board text added: "500mA MAX"
- board text added: "BCN3D Technologies BCN3D Electronics MainBoard"
- board text added: "BCN3D Technologies BCN3D Electronics MainBoard v1.0 Designed in Barcelona ___________________ Sep 2015 - REV_E"
- board text added: "CLK"
- board text added: "E0"
- board text added: "E1"
- board text added: "For more info scan QR Code"
- board text added: "HB"
- board text added: "Jumper to 5V"
- board text added: "MI"
- board text added: "MO"
- board text added: "QR sticker here!"
- board text added: "RST"
- board text added: "SCL"
- board text added: "SDA"
- board text added: "SS"
- board text added: "THERM"
- board text added: "X0"
- board text added: "X1"
- board text added: "Y0"
- board text added: "Z"
- board text added: "blue"
- board text added: "grn"
- board text added: "k"
- board text added: "red"
- board text removed: "+"
- board text removed: "-"
- board text removed: "1"
- board text removed: "19"
- board text removed: "2"
- board text removed: "20"
- board text removed: "BCN3D Electronics MainBoard v1.0 Designed in Barcelona ___________________ MotherBoard - Jan 2015 Marc Cobler - REV_B ___________________"
- board text removed: "SD & LCD"
- board text removed: "_________________________ BCN3D Electronics Fundacio CIM"
